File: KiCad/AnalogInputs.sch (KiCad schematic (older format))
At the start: 50 parts, among them J10 AI2, J11 AI3, J12 AI4, J13 AI5, J14 AI6, J15 AI7, J16 AI8, J17 AI9, J18 A10, J9 AI1

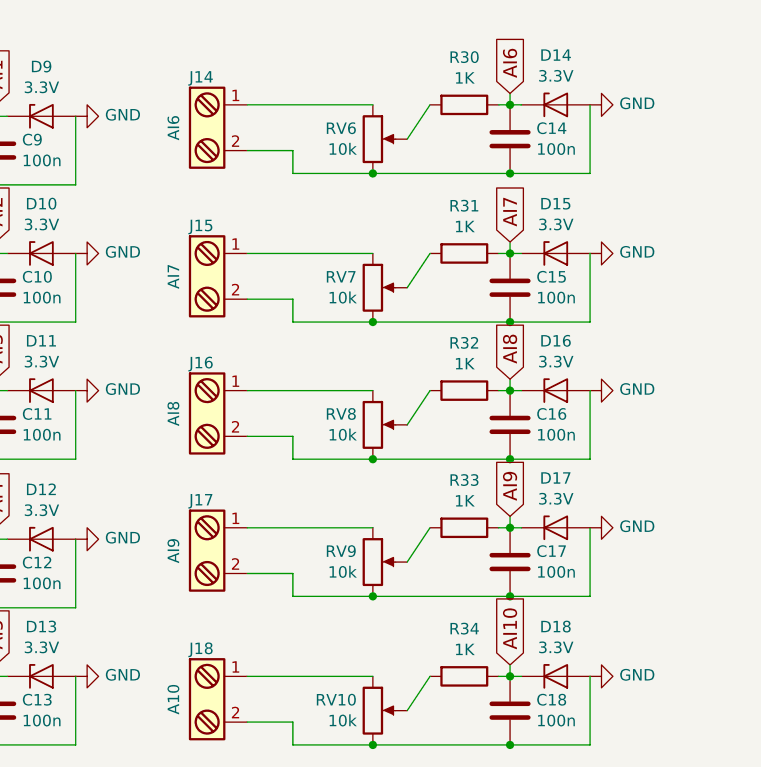
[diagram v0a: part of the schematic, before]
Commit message: Added power supply
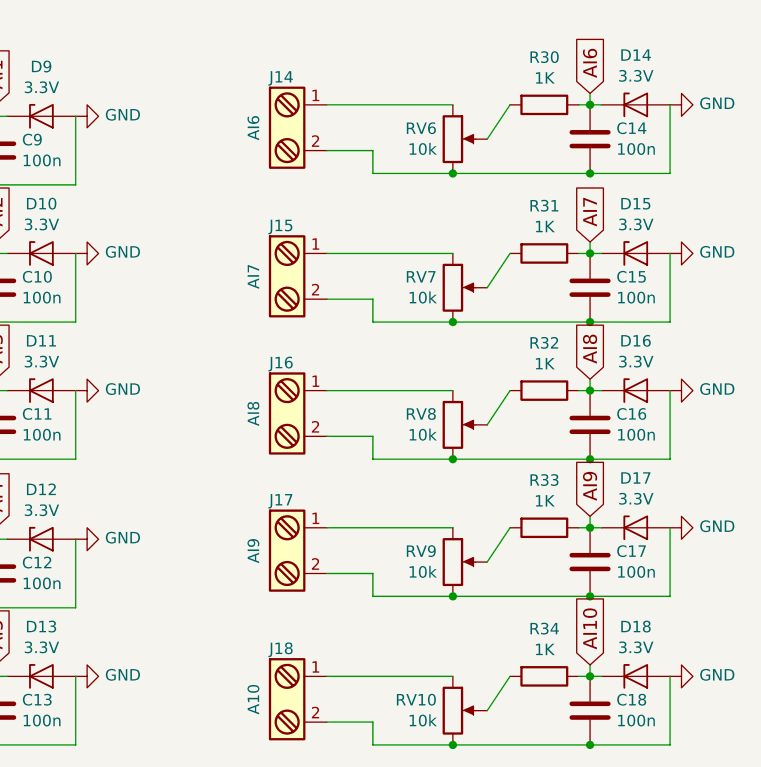
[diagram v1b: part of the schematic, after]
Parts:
- D10, D11, D12, D13, D14, D15, D16, D17, D18, D9: footprint SMD:D_SOT-23 -> Diodes_SMD:D_SOT-23_ANK
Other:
- moved on the sheet: C14, C15, C16, C17, C18, D14, D15, D16, D17, D18, J14, J15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

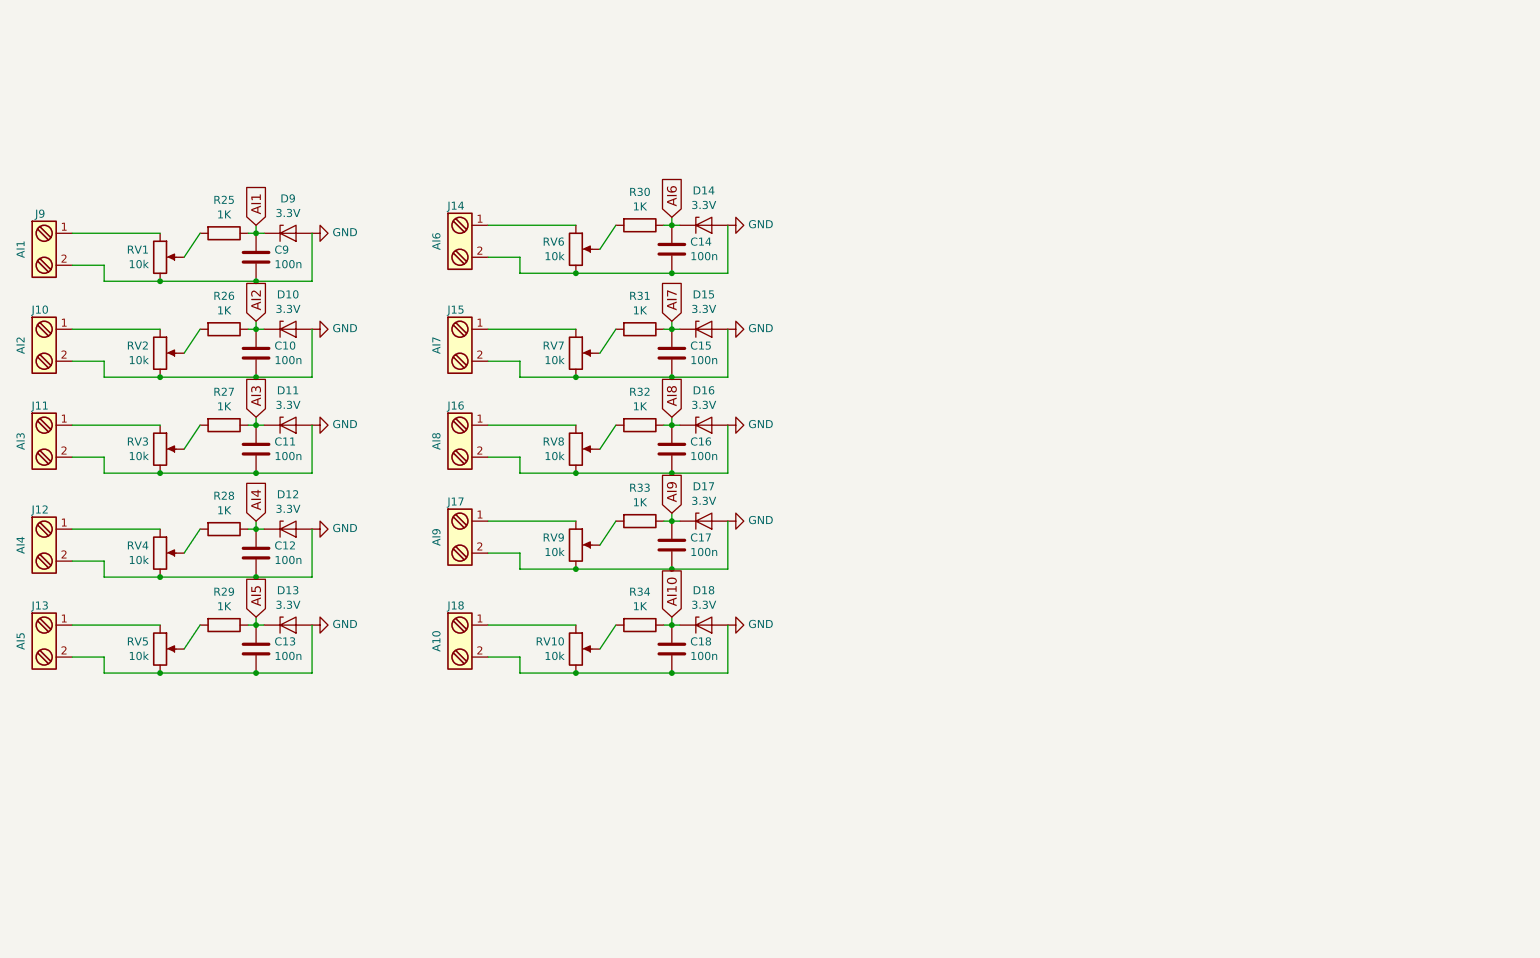
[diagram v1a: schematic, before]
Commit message: Use I2C for I/O
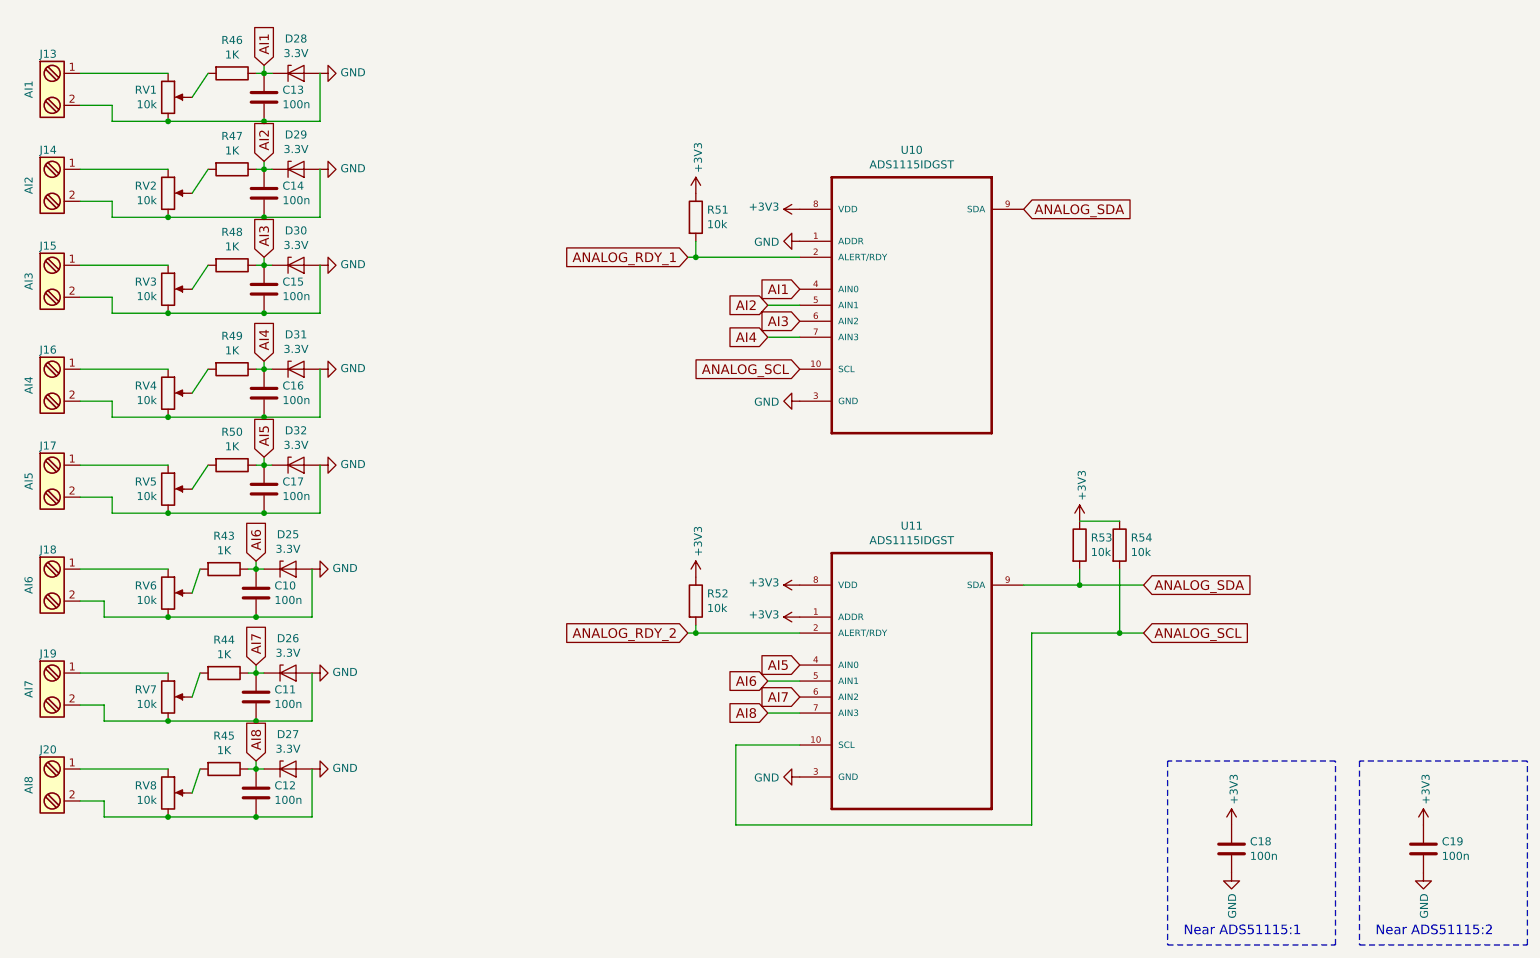
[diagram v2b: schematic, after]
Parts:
- removed C17: 100n, Capacitors_SMD:C_0805, symbol C
- removed D17, D18: 3.3V, Diodes_SMD:D_SOT-23_ANK, symbol D_Zener
- removed J17: AI9, Connectors_Terminal_Blocks:TerminalBlock_Pheonix_MPT-2.54mm_2pol, symbol Screw_Terminal_1x02
- removed J18: A10, Connectors_Terminal_Blocks:TerminalBlock_Pheonix_MPT-2.54mm_2pol, symbol Screw_Terminal_1x02
- removed R33, R34: 1K, Resistors_SMD:R_0805, symbol R
- removed RV10, RV9: 10k, Potentiometers:Potentiometer_WirePads_Small, symbol POT
- added C19: 100n, Capacitors_SMD:C_0805, symbol C
- added R51, R52, R53, R54: 10k, Resistors_SMD:R_0805, symbol R
- added U10, U11: ADS1115IDGST, ADS1115IDGST:SOP50P490X110-10N, symbol ADS1115IDGST
- renumbered C14 to C10, C15 to C11, C16 to C12, C9 to C13, C10 to C14, C11 to C15, C12 to C16, C13 to C17, D14 to D25, D15 to D26, D16 to D27, D9 to D28, D10 to D29, D11 to D30, D12 to D31, D13 to D32, J9 to J13, J10 to J14, J11 to J15, J12 to J16, J13 to J17, J14 to J18, J15 to J19, J16 to J20, R30 to R43, R31 to R44, R32 to R45, R25 to R46, R26 to R47, R27 to R48, R28 to R49, R29 to R50
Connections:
- net AI1: now also U10.4 (AIN0)
- net AI2: now also U10.5 (AIN1)
- net AI3: now also U10.6 (AIN2)
- net AI4: now also U10.7 (AIN3)
- net AI5: now also U11.4 (AIN0)
- net AI6: now also U11.5 (AIN1)
- net AI7: now also U11.6 (AIN2)
- net AI8: now also U11.7 (AIN3)
- net GND: now also C19.2, U10.1 (ADDR), U10.3 (GND), U11.3 (GND)
- net AI10 renamed +3V3
- net +3V3: now also C19.1, R51.1, R52.1, R53.1, R54.1, U10.8 (VDD), U11.1 (ADDR), U11.8 (VDD)
- new net ANALOG_RDY_1: R51.2, U10.2 (ALERT/RDY)
- new net ANALOG_RDY_2: R52.2, U11.2 (ALERT/RDY)
- new net ANALOG_SCL: R54.2, U10.10 (SCL), U11.10 (SCL)
- new net ANALOG_SDA: R53.2, U10.9 (SDA), U11.9 (SDA)
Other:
- note added: "Near ADS51115:1"
- note added: "Near ADS51115:2"
- moved on the sheet: C10, C11, C12, C13, C14, C15, C16, C17, D25, D26, D27, D28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

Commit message: Reworked power-supply to provide 5V. Updated ESP-connections.
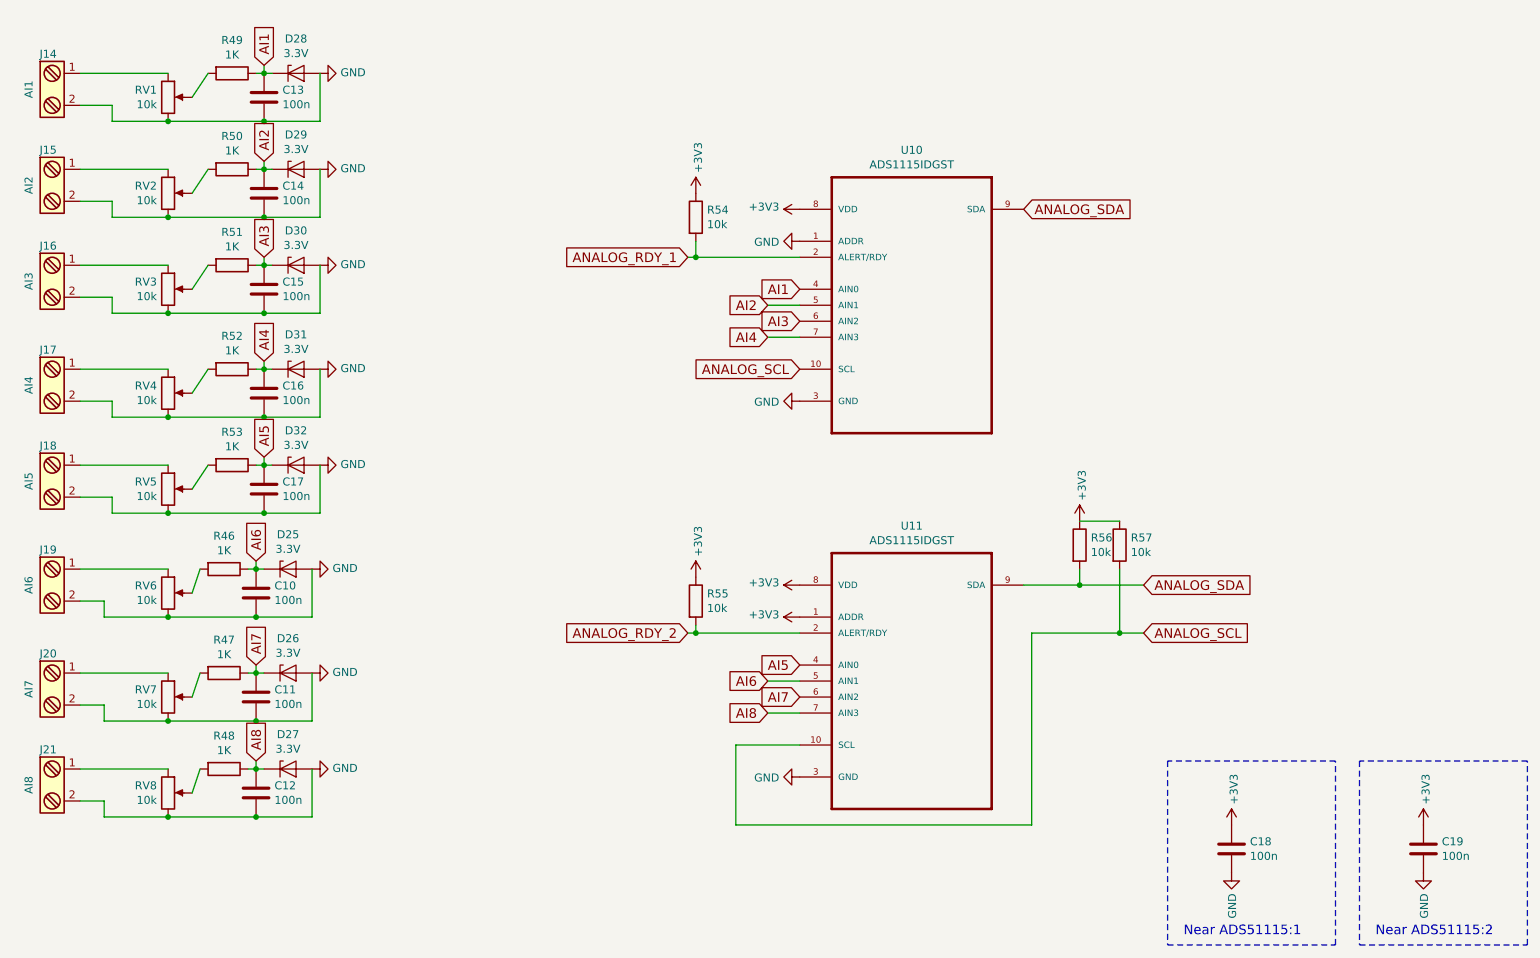
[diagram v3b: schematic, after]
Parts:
- renumbered J13 to J14, J14 to J15, J15 to J16, J16 to J17, J17 to J18, J18 to J19, J19 to J20, J20 to J21, R43 to R46, R44 to R47, R45 to R48, R46 to R49, R47 to R50, R48 to R51, R49 to R52, R50 to R53, R51 to R54, R52 to R55, R53 to R56, R54 to R57

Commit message: More work
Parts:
- renumbered C13 to C401, C14 to C402, C15 to C403, C16 to C404, C17 to C405, C10 to C406, C11 to C407, C12 to C408, C18 to C409, C19 to C410, D28 to D401, D29 to D402, D30 to D403, D31 to D404, D32 to D405, D25 to D406, D26 to D407, D27 to D408, J14 to J401, J15 to J402, J16 to J403, J17 to J404, J18 to J405, J19 to J406, J20 to J407, J21 to J408, R46 to R401, R47 to R402, R48 to R403, R49 to R404, R50 to R405, R51 to R406, R52 to R407, R53 to R408, R54 to R409, R55 to R410, R56 to R411, R57 to R412, RV1 to RV401, RV2 to RV402, RV3 to RV403, RV4 to RV404, RV5 to RV405, RV6 to RV406, RV7 to RV407, RV8 to RV408, U10 to U401, U11 to U402
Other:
- moved on the sheet: C406, C407, C408, C409, C410, D406, D407, D408, R401, R402, R403

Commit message: More layout
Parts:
- renumbered C410 to C409, C409 to C410, R404 to R401, R405 to R402, R406 to R403, R407 to R404, R408 to R405, R401 to R406, R402 to R407, R403 to R408
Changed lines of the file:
@@
 $EndComp
 $Comp
-L R R404
+L R R401
 U 1 1 591B4BA6
 P 2850 900
-F 0 "R404" V 2643 900 50  0000 C CNN
+F 0 "R401" V 2643 900 50  0000 C CNN
 F 1 "1K" V 2734 900 50  0000 C CNN
 F 2 "Resistors_SMD:R_0805" V 2780 900 50  0001 C CNN
@@
 $EndComp
 $Comp
-L GND #PWR051
+L GND #PWR401
 U 1 1 591B4F3C
 P 3400 900
-F 0 "#PWR051" H 3400 650 50  0001 C CNN
+F 0 "#PWR401" H 3400 650 50  0001 C CNN
 F 1 "GND" V 3405 772 50  0000 R CNN
 F 2 "" H 3400 900 50  0001 C CNN
@@
 $EndComp
 $Comp
-L R R405
+L R R402
 U 1 1 591C78E9
 P 2850 1500
-F 0 "R405" V 2643 1500 50  0000 C CNN
+F 0 "R402" V 2643 1500 50  0000 C CNN
 F 1 "1K" V 2734 1500 50  0000 C CNN
 F 2 "Resistors_SMD:R_0805" V 2780 1500 50  0001 C CNN
@@
 $EndComp
 $Comp
-L GND #PWR052
+L GND #PWR402
 U 1 1 591C78F7
 P 3400 1500
-F 0 "#PWR052" H 3400 1250 50  0001 C CNN
+F 0 "#PWR402" H 3400 1250 50  0001 C CNN
 F 1 "GND" V 3405 1372 50  0000 R CNN
 F 2 "" H 3400 1500 50  0001 C CNN
@@
 $EndComp
 $Comp
-L R R406
+L R R403
 U 1 1 591C7A00
 P 2850 2100
-F 0 "R406" V 2643 2100 50  0000 C CNN
+F 0 "R403" V 2643 2100 50  0000 C CNN
 F 1 "1K" V 2734 2100 50  0000 C CNN
 F 2 "Resistors_SMD:R_0805" V 2780 2100 50  0001 C CNN
@@
 $EndComp
 $Comp
-L GND #PWR053
+L GND #PWR403
 U 1 1 591C7A0E
 P 3400 2100
-F 0 "#PWR053" H 3400 1850 50  0001 C CNN
+F 0 "#PWR403" H 3400 1850 50  0001 C CNN
 F 1 "GND" V 3405 1972 50  0000 R CNN
 F 2 "" H 3400 2100 50  0001 C CNN
@@
 $EndComp
 $Comp
-L R R407
+L R R404
 U 1 1 591C93AA
 P 2850 2750
-F 0 "R407" V 2643 2750 50  0000 C CNN
+F 0 "R404" V 2643 2750 50  0000 C CNN
 F 1 "1K" V 2734 2750 50  0000 C CNN
 F 2 "Resistors_SMD:R_0805" V 2780 2750 50  0001 C CNN
@@
 $EndComp
 $Comp
-L GND #PWR054
+L GND #PWR404
 U 1 1 591C93B8
 P 3400 2750
-F 0 "#PWR054" H 3400 2500 50  0001 C CNN
+F 0 "#PWR404" H 3400 2500 50  0001 C CNN
 F 1 "GND" V 3405 2622 50  0000 R CNN
 F 2 "" H 3400 2750 50  0001 C CNN
@@
 $EndComp
 $Comp
-L R R408
+L R R405
 U 1 1 591C9766
 P 2850 3350
-F 0 "R408" V 2643 3350 50  0000 C CNN
+F 0 "R405" V 2643 3350 50  0000 C CNN
 F 1 "1K" V 2734 3350 50  0000 C CNN
 F 2 "Resistors_SMD:R_0805" V 2780 3350 50  0001 C CNN
@@
 $EndComp
 $Comp
-L GND #PWR055
+L GND #PWR405
 U 1 1 591C9774
 P 3400 3350
-F 0 "#PWR055" H 3400 3100 50  0001 C CNN
+F 0 "#PWR405" H 3400 3100 50  0001 C CNN
 F 1 "GND" V 3405 3222 50  0000 R CNN
 F 2 "" H 3400 3350 50  0001 C CNN
@@
 $EndComp
 $Comp
-L R R401
+L R R406
 U 1 1 591C993C
 P 2850 4000
-F 0 "R401" V 2643 4000 50  0000 C CNN
+F 0 "R406" V 2643 4000 50  0000 C CNN
 F 1 "1K" V 2734 4000 50  0000 C CNN
 F 2 "Resistors_SMD:R_0805" V 2780 4000 50  0001 C CNN
@@
 $EndComp
 $Comp
-L GND #PWR056
+L GND #PWR406
 U 1 1 591C994A
 P 3400 4000
-F 0 "#PWR056" H 3400 3750 50  0001 C CNN
+F 0 "#PWR406" H 3400 3750 50  0001 C CNN
 F 1 "GND" V 3405 3872 50  0000 R CNN
 F 2 "" H 3400 4000 50  0001 C CNN
@@
 $EndComp
 $Comp
-L R R402
+L R R407
 U 1 1 591C9FDB
 P 2850 4650
-F 0 "R402" V 2643 4650 50  0000 C CNN
+F 0 "R407" V 2643 4650 50  0000 C CNN
 F 1 "1K" V 2734 4650 50  0000 C CNN
 F 2 "Resistors_SMD:R_0805" V 2780 4650 50  0001 C CNN
@@
 $EndComp
 $Comp
-L GND #PWR057
+L GND #PWR407
 U 1 1 591C9FE9
 P 3400 4650
-F 0 "#PWR057" H 3400 4400 50  0001 C CNN
+F 0 "#PWR407" H 3400 4400 50  0001 C CNN
 F 1 "GND" V 3405 4522 50  0000 R CNN
 F 2 "" H 3400 4650 50  0001 C CNN
@@
 $EndComp
 $Comp
-L R R403
+L R R408
 U 1 1 591CA106
 P 2850 5250
-F 0 "R403" V 2643 5250 50  0000 C CNN
+F 0 "R408" V 2643 5250 50  0000 C CNN
 F 1 "1K" V 2734 5250 50  0000 C CNN
 F 2 "Resistors_SMD:R_0805" V 2780 5250 50  0001 C CNN
@@
 $EndComp
 $Comp
-L GND #PWR058
+L GND #PWR408
 U 1 1 591CA114
 P 3400 5250
-F 0 "#PWR058" H 3400 5000 50  0001 C CNN
+F 0 "#PWR408" H 3400 5000 50  0001 C CNN
 F 1 "GND" V 3405 5122 50  0000 R CNN
 F 2 "" H 3400 5250 50  0001 C CNN
@@
 AI8
 $Comp
-L +3V3 #PWR059
+L +3V3 #PWR411
 U 1 1 5921C734
 P 6400 1750
-F 0 "#PWR059" H 6400 1600 50  0001 C CNN
+F 0 "#PWR411" H 6400 1600 50  0001 C CNN
 F 1 "+3V3" V 6415 1878 50  0000 L CNN
 F 2 "" H 6400 1750 50  0001 C CNN
@@
 $EndComp
 $Comp
-L +3V3 #PWR060
+L +3V3 #PWR414
 U 1 1 5921D0CA
 P 6400 4100
-F 0 "#PWR060" H 6400 3950 50  0001 C CNN
+F 0 "#PWR414" H 6400 3950 50  0001 C CNN
 F 1 "+3V3" V 6415 4228 50  0000 L CNN
 F 2 "" H 6400 4100 50  0001 C CNN
@@
 $EndComp
 $Comp
-L GND #PWR061
+L GND #PWR416
 U 1 1 5921DD8E
 P 6400 5300
-F 0 "#PWR061" H 6400 5050 50  0001 C CNN
+F 0 "#PWR416" H 6400 5050 50  0001 C CNN
 F 1 "GND" V 6405 5172 50  0000 R CNN
 F 2 "" H 6400 5300 50  0001 C CNN
@@
 $EndComp
 $Comp
-L GND #PWR062
+L GND #PWR413
 U 1 1 5921DE1E
 P 6400 2950
-F 0 "#PWR062" H 6400 2700 50  0001 C CNN
+F 0 "#PWR413" H 6400 2700 50  0001 C CNN
 F 1 "GND" V 6405 2822 50  0000 R CNN
 F 2 "" H 6400 2950 50  0001 C CNN
@@
 $EndComp
 $Comp
-L GND #PWR063
+L GND #PWR412
 U 1 1 5921EEA8
 P 6400 1950
-F 0 "#PWR063" H 6400 1700 50  0001 C CNN
+F 0 "#PWR412" H 6400 1700 50  0001 C CNN
 F 1 "GND" V 6405 1822 50  0000 R CNN
 F 2 "" H 6400 1950 50  0001 C CNN
@@
 $EndComp
 $Comp
-L +3V3 #PWR064
+L +3V3 #PWR415
 U 1 1 5921EF38
 P 6400 4300
-F 0 "#PWR064" H 6400 4150 50  0001 C CNN
+F 0 "#PWR415" H 6400 4150 50  0001 C CNN
 F 1 "+3V3" V 6415 4428 50  0000 L CNN
 F 2 "" H 6400 4300 50  0001 C CNN
@@
 Connection ~ 5750 2050
 $Comp
-L +3V3 #PWR065
+L +3V3 #PWR409
 U 1 1 592BD70B
 P 5750 1650
-F 0 "#PWR065" H 5750 1500 50  0001 C CNN
+F 0 "#PWR409" H 5750 1500 50  0001 C CNN
 F 1 "+3V3" V 5765 1778 50  0000 L CNN
 F 2 "" H 5750 1650 50  0001 C CNN
@@
 Connection ~ 5750 4400
 $Comp
-L +3V3 #PWR066
+L +3V3 #PWR410
 U 1 1 592BDFDB
 P 5750 4050
-F 0 "#PWR066" H 5750 3900 50  0001 C CNN
+F 0 "#PWR410" H 5750 3900 50  0001 C CNN
 F 1 "+3V3" V 5765 4178 50  0000 L CNN
 F 2 "" H 5750 4050 50  0001 C CNN
@@
 $EndComp
 $Comp
-L +3V3 #PWR067
+L +3V3 #PWR417
 U 1 1 592C06FF
 P 8150 3700
-F 0 "#PWR067" H 8150 3550 50  0001 C CNN
+F 0 "#PWR417" H 8150 3550 50  0001 C CNN
 F 1 "+3V3" V 8165 3828 50  0000 L CNN
 F 2 "" H 8150 3700 50  0001 C CNN
@@
 	8400 3700 8150 3700
 $Comp
-L C C409
+L C C410
 U 1 1 592CB98A
 P 9100 2350
-F 0 "C409" H 9215 2396 50  0000 L CNN
+F 0 "C410" H 9215 2396 50  0000 L CNN
 F 1 "100n" H 9215 2305 50  0000 L CNN
 F 2 "Capacitors_SMD:C_0805" H 9138 2200 50  0001 C CNN
@@
 $EndComp
 $Comp
-L GND #PWR068
+L GND #PWR421
 U 1 1 592CBB1F
 P 9100 2500
-F 0 "#PWR068" H 9100 2250 50  0001 C CNN
+F 0 "#PWR421" H 9100 2250 50  0001 C CNN
 F 1 "GND" V 9105 2372 50  0000 R CNN
 F 2 "" H 9100 2500 50  0001 C CNN
@@
 $EndComp
 $Comp
-L +3V3 #PWR069
+L +3V3 #PWR420
 U 1 1 592CBC15
 P 9100 2200
-F 0 "#PWR069" H 9100 2050 50  0001 C CNN
+F 0 "#PWR420" H 9100 2050 50  0001 C CNN
 F 1 "+3V3" V 9115 2328 50  0000 L CNN
 F 2 "" H 9100 2200 50  0001 C CNN
@@
 	9750 1800 8700 1800
 $Comp
-L C C410
+L C C409
 U 1 1 592CDFF1
 P 8700 5300
-F 0 "C410" H 8815 5346 50  0000 L CNN
+F 0 "C409" H 8815 5346 50  0000 L CNN
 F 1 "100n" H 8815 5255 50  0000 L CNN
 F 2 "Capacitors_SMD:C_0805" H 8738 5150 50  0001 C CNN
@@
 $EndComp
 $Comp
-L GND #PWR070
+L GND #PWR419
 U 1 1 592CDFF7
 P 8700 5450
-F 0 "#PWR070" H 8700 5200 50  0001 C CNN
+F 0 "#PWR419" H 8700 5200 50  0001 C CNN
 F 1 "GND" V 8705 5322 50  0000 R CNN
 F 2 "" H 8700 5450 50  0001 C CNN
@@
 $EndComp
 $Comp
-L +3V3 #PWR071
+L +3V3 #PWR418
 U 1 1 592CDFFD
 P 8700 5150
-F 0 "#PWR071" H 8700 5000 50  0001 C CNN
+F 0 "#PWR418" H 8700 5000 50  0001 C CNN
 F 1 "+3V3" V 8715 5278 50  0000 L CNN
 F 2 "" H 8700 5150 50  0001 C CNN
